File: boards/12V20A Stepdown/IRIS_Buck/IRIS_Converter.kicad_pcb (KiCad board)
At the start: 4 copper layers, 50 x 40 mm, 27 parts, among them J1 TB005-762-02BE, J2 TB005-762-02BE, Q1 CSD17571Q2, Q2 CSD16340Q3, U1 LM25145RGYR

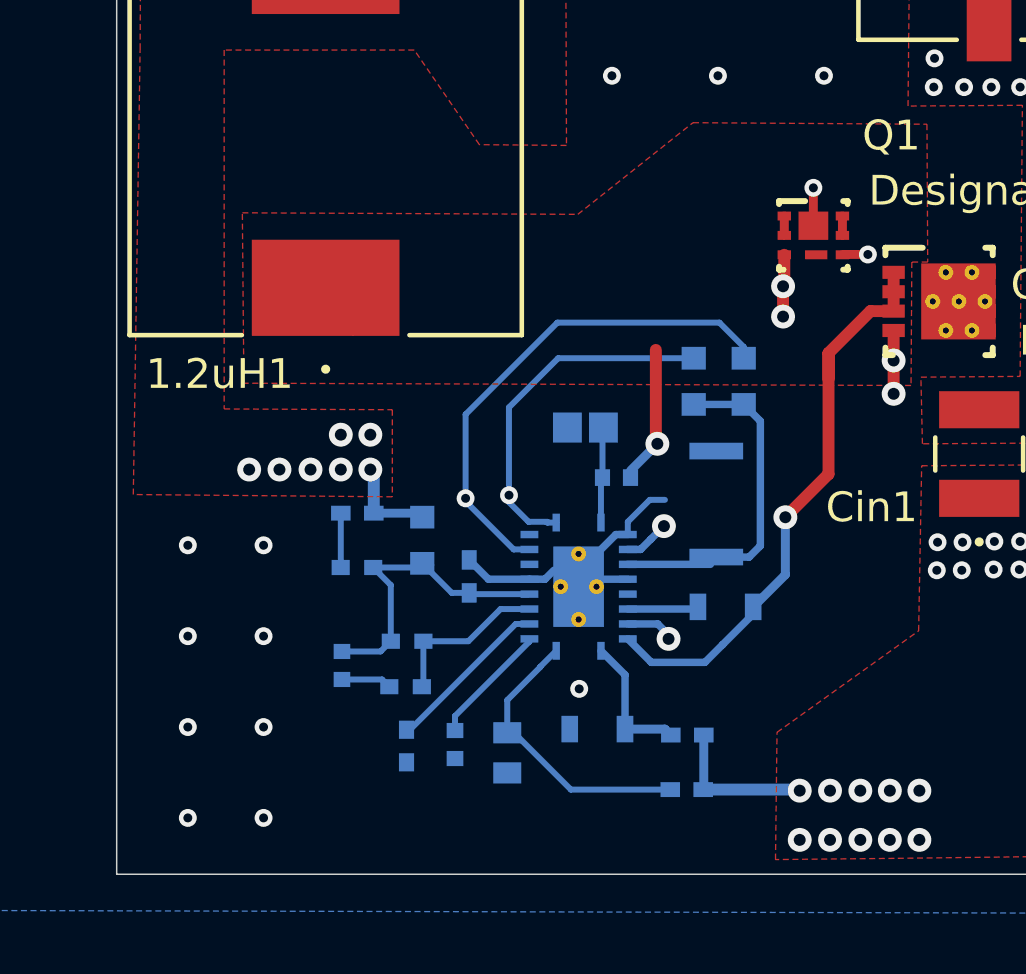
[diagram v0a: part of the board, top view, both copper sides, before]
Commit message: tweaked mosfte orientation and placement
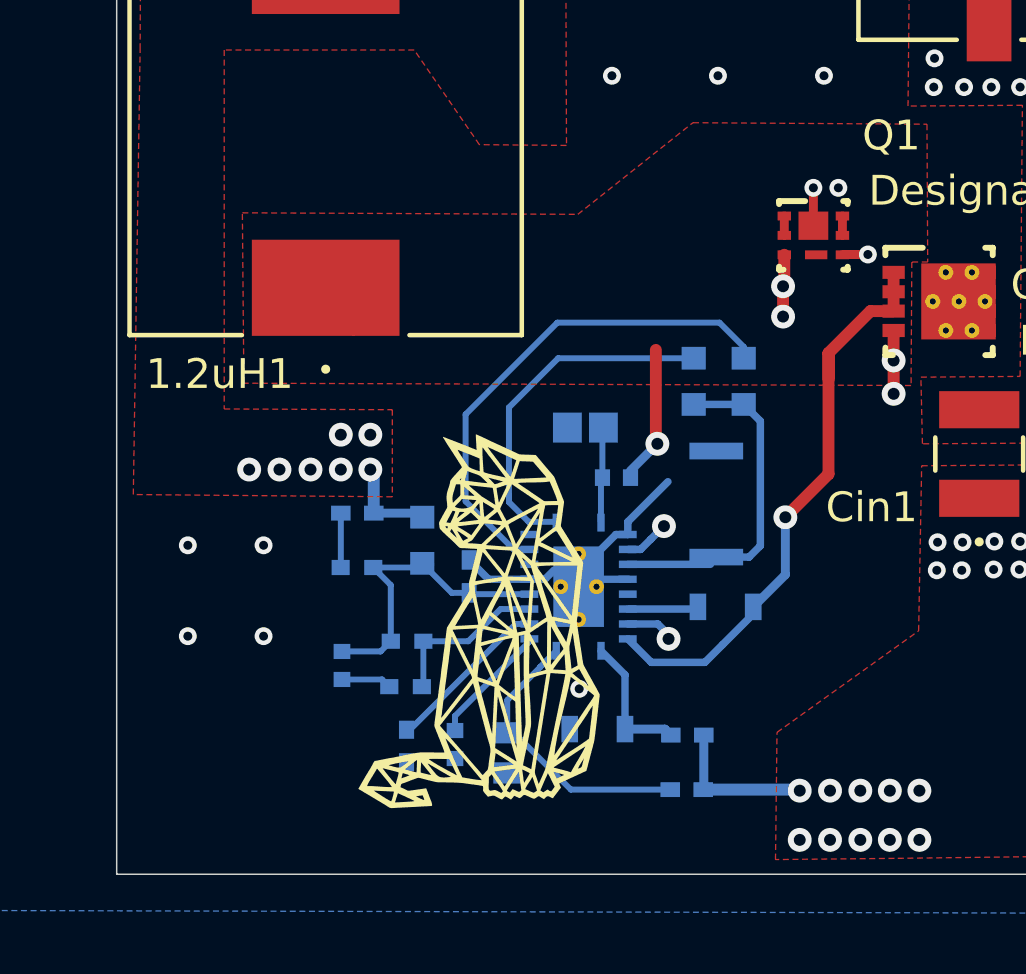
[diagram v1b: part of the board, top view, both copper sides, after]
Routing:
- net GND: track 13.0 -> 13.4 mm, vias 65 -> 62
- net Net-(U1-PGOOD): vias 1 -> 0
- net /SYNCin: vias 1 -> 0

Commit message: Added mounting holes and generated manu files
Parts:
- added REF**: MountingHole_3.2mm_M3, MountingHole:MountingHole_3.2mm_M3, F.Cu at (124.0, 42.6)
- added REF**: MountingHole_3.2mm_M3, MountingHole:MountingHole_3.2mm_M3, F.Cu at (124.0, 75.7)
- added REF**: MountingHole_3.2mm_M3, MountingHole:MountingHole_3.2mm_M3, F.Cu at (79.8, 42.6)
- added REF**: MountingHole_3.2mm_M3, MountingHole:MountingHole_3.2mm_M3, F.Cu at (79.8, 75.7)
- moved J2 11.2 mm to (112.3, 51.6), turned to 90 degrees
- moved J1 10.3 mm to (112.3, 73.9), turned to 90 degrees
- moved Cout1 3.00 mm to (101.6, 46.7)
- moved 1.2uH1 0.49 mm to (82.8, 54.0)
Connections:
- J1 pad 1: GND -> /Vin
- J1 pad 2: /Vin -> GND
- J2 pad 1: /Vout -> GND
- J2 pad 2: GND -> /Vout
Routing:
- net GND: vias 62 -> 56
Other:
- board size 50 x 40 mm -> 52.5 x 42 mm
